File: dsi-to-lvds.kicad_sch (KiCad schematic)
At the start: 22 parts, among them Q8 PJE138K, U2 NTS0104_DHVQFN, U3 SN65DSI84

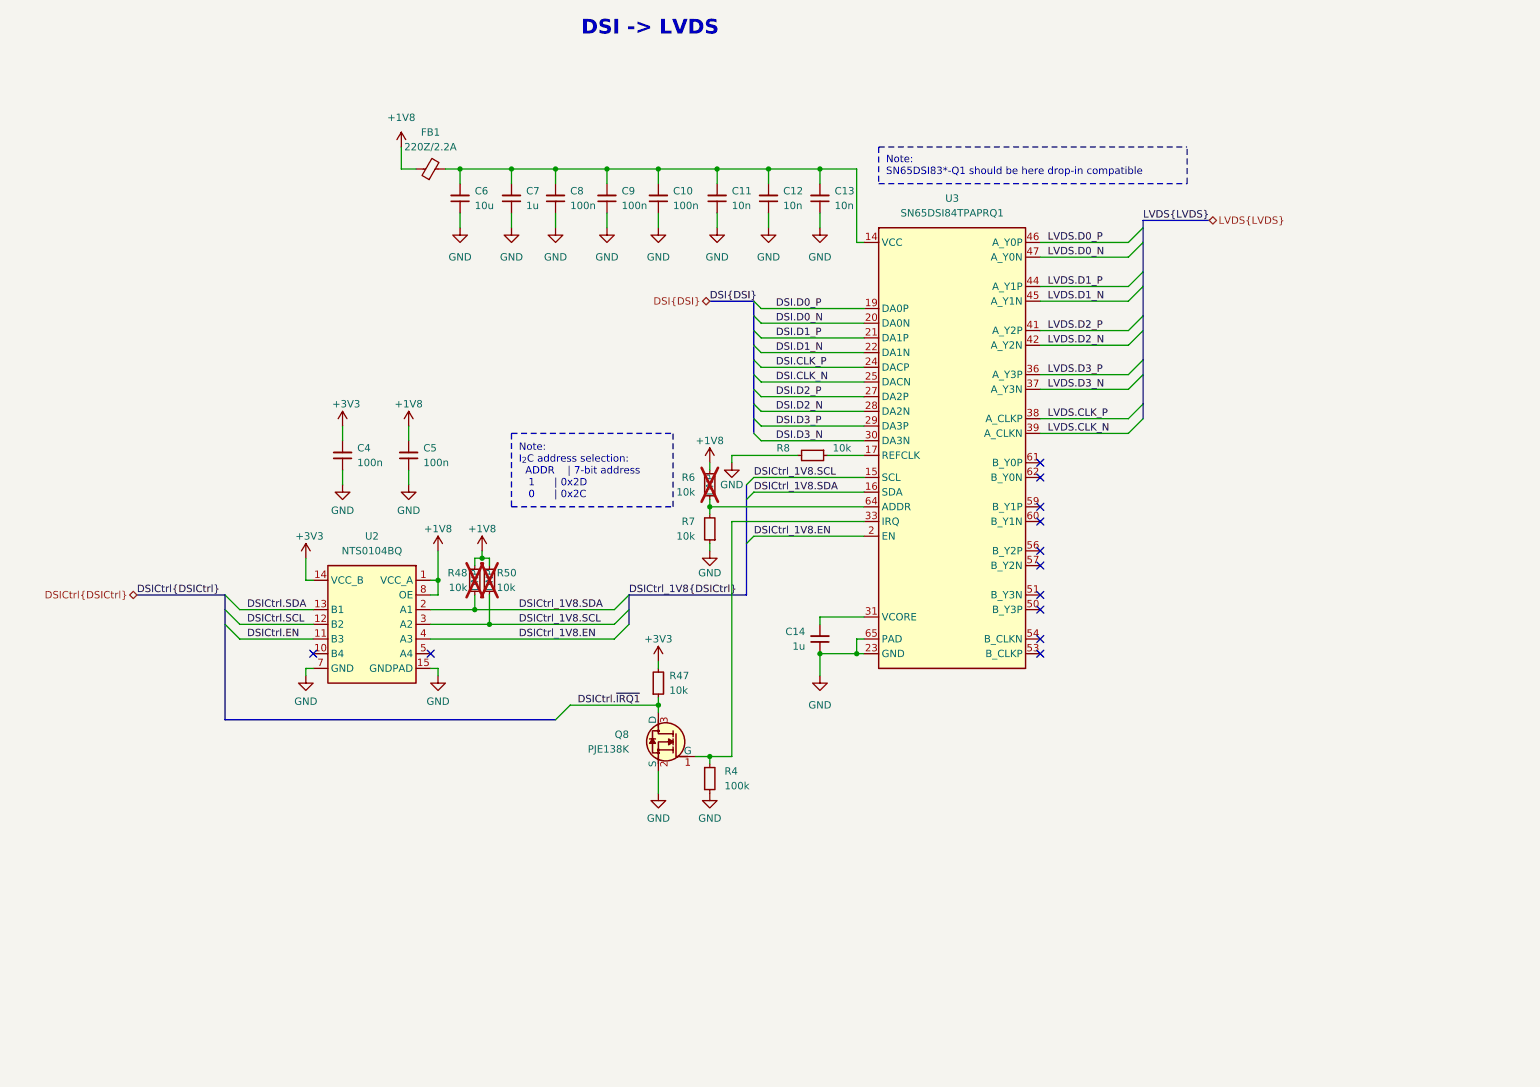
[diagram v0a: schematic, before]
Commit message: [#73840] Bump rev to 1.1.3, Standarize Sch
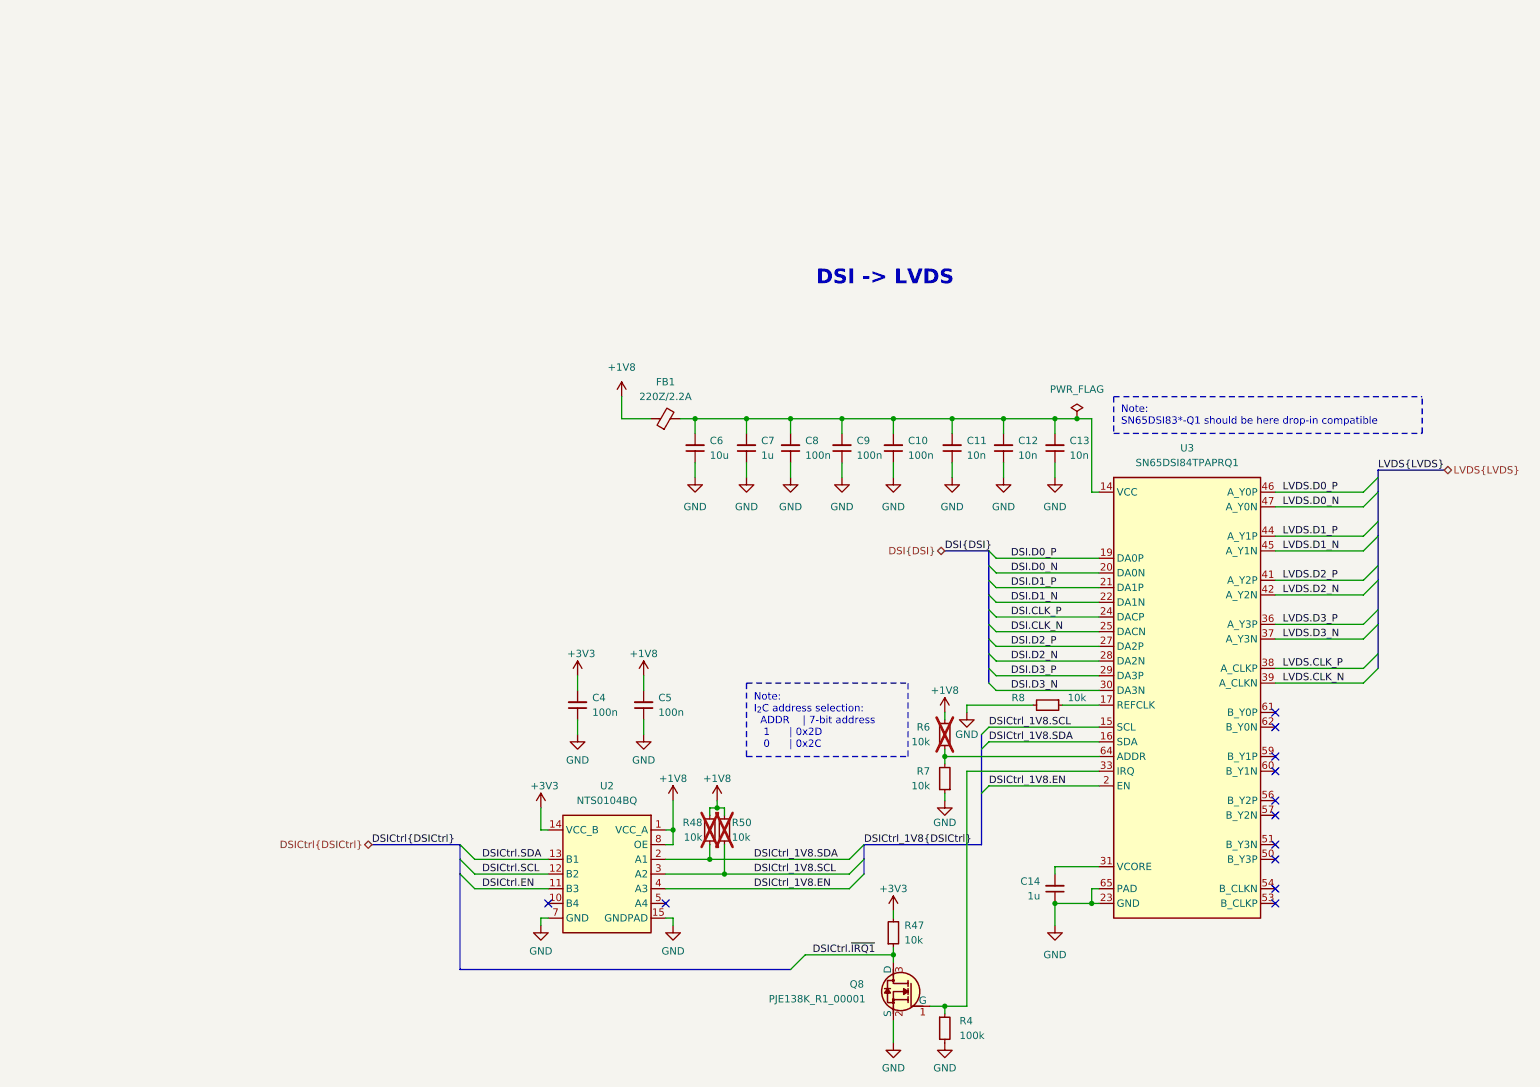
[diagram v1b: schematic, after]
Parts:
- C10, C11, C12, C13, C14, C4, C5, C6, C7, C8, C9, FB1, R4, R47, R7, R8: Public False -> (none)
- R48, R50, R6: DNP DNP -> (none); Public False -> (none); now in the parts list
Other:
- moved on the sheet: C10, C11, C12, C13, C14, C4, C5, C6, C7, C8, C9, FB1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

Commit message: [#86029] Save with KiCad 9
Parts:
- R48, R50, R6: now left out of the parts list
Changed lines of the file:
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@@
 (kicad_sch
-	(version 20231120)
+	(version 20250114)
 	(generator "eeschema")
-	(generator_version "8.0")
+	(generator_version "9.0")
 	(paper "A3")
 	(title_block
@@
 		(comment 1 "www.antmicro.com")
 	)
+	(text "Note:\nI_{2}C address selection:\n  ADDR	| 7-bit address\n   1  	| 0x2D\n   0  	| 0x2C"
+		(exclude_from_sim no)
+		(at 173.99 152.4 0)
+		(effects
+			(font
+				(size 1.27 1.27)
+			)
+			(justify left bottom)
+		)
+	)
+	(text "DSI -> LVDS"
+		(exclude_from_sim no)
+		(at 184.785 72.39 0)
+		(effects
+			(font
+				(size 2.54 2.54)
+				(thickness 0.508)
+				(bold yes)
+			)
+			(justify left bottom)
+		)
+	)
+	(text "Note:\nSN65DSI83*-Q1 should be here drop-in compatible"
+		(exclude_from_sim no)
+		(at 237.49 96.52 0)
+		(effects
+			(font
+				(size 1.27 1.27)
+			)
+			(justify left bottom)
+		)
+	)
 	(junction
 		(at 207.01 196.85)
@@
 		)
 	)
-	(text "Note:\nI_{2}C address selection:\n  ADDR	| 7-bit address\n   1  	| 0x2D\n   0  	| 0x2C"
-		(exclude_from_sim no)
-		(at 173.99 152.4 0)
-		(effects
-			(font
-				(size 1.27 1.27)
-			)
-			(justify left bottom)
-		)
-	)
-	(text "DSI -> LVDS"
-		(exclude_from_sim no)
-		(at 184.785 72.39 0)
-		(effects
-			(font
-				(size 2.54 2.54)
-				(thickness 0.508)
-				(bold yes)
-			)
-			(justify left bottom)
-		)
-	)
-	(text "Note:\nSN65DSI83*-Q1 should be here drop-in compatible"
-		(exclude_from_sim no)
-		(at 237.49 96.52 0)
-		(effects
-			(font
-				(size 1.27 1.27)
-			)
-			(justify left bottom)
-		)
-	)
 	(label "DSICtrl_1V8.EN"
 		(at 173.99 176.53 0)
-		(fields_autoplaced yes)
 		(effects
 			(font
@@
 	(label "DSICtrl_1V8.SCL"
 		(at 173.99 173.99 0)
-		(fields_autoplaced yes)
 		(effects
 			(font
@@
 	(label "DSI.D2_N"
 		(at 218.44 137.16 0)
-		(fields_autoplaced yes)
 		(effects
 			(font
@@
 	(label "LVDS.D1_P"
 		(at 265.43 115.57 0)
-		(fields_autoplaced yes)
 		(effects
 			(font
@@
 	(label "LVDS.D3_N"
 		(at 265.43 133.35 0)
-		(fields_autoplaced yes)
 		(effects
 			(font
@@
 	(label "DSICtrl_1V8.SCL"
 		(at 214.63 148.59 0)
-		(fields_autoplaced yes)
 		(effects
 			(font
@@
 	(label "DSI.D3_P"
 		(at 218.44 139.7 0)
-		(fields_autoplaced yes)
 		(effects
 			(font
@@
 	(label "DSI.D2_P"
 		(at 218.44 134.62 0)
-		(fields_autoplaced yes)
 		(effects
 			(font
@@
 	(label "DSICtrl.SCL"
 		(at 127 173.99 0)
-		(fields_autoplaced yes)
 		(effects
 			(font
@@
 	(label "LVDS.D0_N"
 		(at 265.43 110.49 0)
-		(fields_autoplaced yes)
 		(effects
 			(font
@@
 	(label "DSI.CLK_N"
 		(at 218.44 132.08 0)
-		(fields_autoplaced yes)
 		(effects
 			(font
@@
 	(label "LVDS.D3_P"
 		(at 265.43 130.81 0)
-		(fields_autoplaced yes)
 		(effects
 			(font
@@
 	(label "LVDS.CLK_N"
 		(at 265.43 140.97 0)
-		(fields_autoplaced yes)
 		(effects
 			(font
@@
 	(label "DSI.D0_P"
 		(at 218.44 119.38 0)
-		(fields_autoplaced yes)
 		(effects
 			(font
@@
 	(label "LVDS.D1_N"
 		(at 265.43 118.11 0)
-		(fields_autoplaced yes)
 		(effects
 			(font
@@
 	(label "DSI.D1_P"
 		(at 218.44 124.46 0)
-		(fields_autoplaced yes)
 		(effects
 			(font
@@
 	(label "LVDS{LVDS}"
 		(at 293.37 104.14 180)
-		(fields_autoplaced yes)
 		(effects
 			(font
@@
 	(label "DSICtrl{DSICtrl}"
 		(at 107.95 168.91 0)
-		(fields_autoplaced yes)
 		(effects
 			(font
@@
 	(label "DSICtrl_1V8.SDA"
 		(at 214.63 151.13 0)
-		(fields_autoplaced yes)
 		(effects
 			(font
@@
 	(label "LVDS.D2_P"
 		(at 265.43 123.19 0)
-		(fields_autoplaced yes)
 		(effects
 			(font
@@
 	(label "DSICtrl_1V8.EN"
 		(at 214.63 158.75 0)
-		(fields_autoplaced yes)
 		(effects
 			(font
@@
 	(label "DSI.CLK_P"
 		(at 218.44 129.54 0)
-		(fields_autoplaced yes)
 		(effects
 			(font
@@
 	(label "DSI.D1_N"
 		(at 218.44 127 0)
-		(fields_autoplaced yes)
 		(effects
 			(font
@@
 	(label "DSICtrl_1V8.SDA"
 		(at 173.99 171.45 0)
-		(fields_autoplaced yes)
 		(effects
 			(font
@@
 	(label "LVDS.D2_N"
 		(at 265.43 125.73 0)
-		(fields_autoplaced yes)
 		(effects
 			(font
@@
 	(label "DSICtrl.EN"
 		(at 127 176.53 0)
-		(fields_autoplaced yes)
 		(effects
 			(font
@@
 	(label "LVDS.D0_P"
 		(at 265.43 107.95 0)
-		(fields_autoplaced yes)
 		(effects
 			(font
@@
 	(label "LVDS.CLK_P"
 		(at 265.43 138.43 0)
-		(fields_autoplaced yes)
 		(effects
 			(font
@@
 	(label "DSICtrl.~{IRQ1}"
 		(at 184.15 187.96 0)
-		(fields_autoplaced yes)
 		(effects
 			(font
@@
 	(label "DSI.D0_N"
 		(at 218.44 121.92 0)
-		(fields_autoplaced yes)
 		(effects
 			(font
@@
 	(label "DSICtrl.SDA"
 		(at 127 171.45 0)
-		(fields_autoplaced yes)
 		(effects
 			(font
@@
 	(label "DSI{DSI}"
 		(at 207.01 118.11 0)
-		(fields_autoplaced yes)
 		(effects
 			(font
@@
 	(label "DSICtrl_1V8{DSICtrl}"
 		(at 193.04 168.91 0)
-		(fields_autoplaced yes)
 		(effects
 			(font
@@
 	(label "DSI.D3_N"
 		(at 218.44 142.24 0)
-		(fields_autoplaced yes)
 		(effects
 			(font
@@
 		(shape bidirectional)
 		(at 293.37 104.14 0)
-		(fields_autoplaced yes)
 		(effects
 			(font
@@
 		(shape bidirectional)
 		(at 107.95 168.91 180)
-		(fields_autoplaced yes)
 		(effects
 			(font
@@
 		(shape bidirectional)
 		(at 207.01 118.11 180)
-		(fields_autoplaced yes)
 		(effects
 			(font
@@
 		(unit 1)
 		(exclude_from_sim no)
-		(in_bom yes)
+		(in_bom no)
 		(on_board yes)
 		(dnp yes)
@@
 		(unit 1)
 		(exclude_from_sim no)
-		(in_bom yes)
+		(in_bom no)
 		(on_board yes)
 		(dnp yes)
@@
 		(unit 1)
 		(exclude_from_sim no)
-		(in_bom yes)
+		(in_bom no)
 		(on_board yes)
 		(dnp yes)
